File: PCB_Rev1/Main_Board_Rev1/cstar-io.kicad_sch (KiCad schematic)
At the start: 11 parts, among them J2 Conn_01x04_Socket, J3 691137710002, Q1 AO3400A, Q2 AO3400A, Q3 AO3400A, Q4 IRFHM9331TRPBF

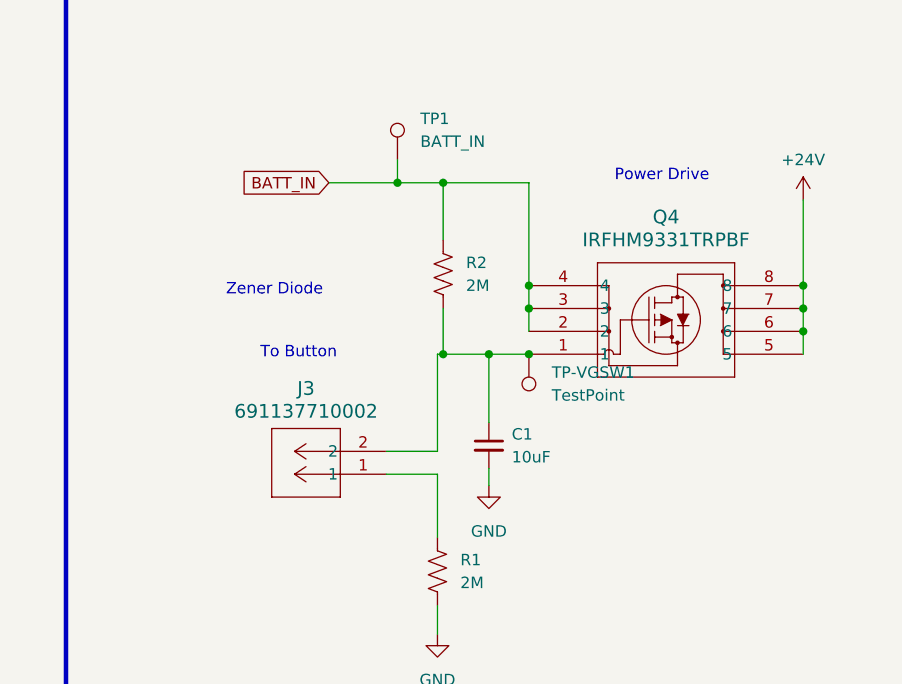
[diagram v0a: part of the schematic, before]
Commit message: I/O footprints added
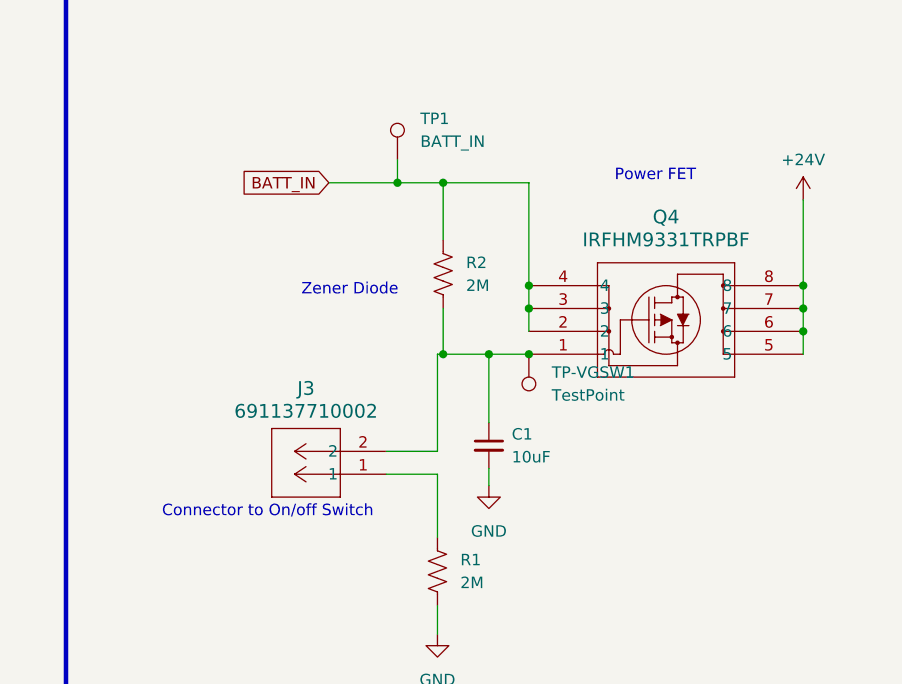
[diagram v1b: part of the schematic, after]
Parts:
- Q1, Q2, Q3: footprint Package_TO_SOT_SMD:SOT-23 -> Footprints:RGB-FETS
- Q4: footprint CSTAR-MainBoard-Footprints:IRFHM9331TRPBF -> Footprints:Power_FET
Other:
- note added: "Connector to On/off Switch"
- note added: "Power FET"
- note removed: "Power Drive"
- note removed: "To Button"
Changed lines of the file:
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@@
 	(text "Zener Diode"
 		(exclude_from_sim no)
-		(at 185.42 64.77 0)
+		(at 193.802 64.77 0)
 		(effects
 			(font
@@
 		)
 	)
-	(text "Power Drive\n"
+	(text "Power FET"
 		(exclude_from_sim no)
 		(at 228.6 52.07 0)
@@
 		)
 	)
-	(text "To Button\n"
-		(exclude_from_sim no)
-		(at 189.23 71.755 0)
+	(text "Connector to On/off Switch"
+		(exclude_from_sim no)
+		(at 178.308 89.408 0)
 		(effects
 			(font
@@
 			)
 		)
-		(property "Footprint" "Package_TO_SOT_SMD:SOT-23"
+		(property "Footprint" "Footprints:RGB-FETS"
 			(at 69.85 62.865 0)
 			(effects
@@
 			)
 		)
-		(property "Footprint" "CSTAR-MainBoard-Footprints:IRFHM9331TRPBF"
+		(property "Footprint" "Footprints:Power_FET"
 			(at 219.075 63.5 0)
 			(effects
@@
 			)
 		)
-		(property "Footprint" "Package_TO_SOT_SMD:SOT-23"
+		(property "Footprint" "Footprints:RGB-FETS"
 			(at 119.38 100.33 0)
 			(effects
@@
 			)
 		)
-		(property "Footprint" "Package_TO_SOT_SMD:SOT-23"
+		(property "Footprint" "Footprints:RGB-FETS"
 			(at 95.25 83.82 0)
 			(effects

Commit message: Added new footprints
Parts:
- J2: footprint CSTAR-MainBoard-Footprints:B4B_PH_K_S -> (none)
- J3: footprint CSTAR-MainBoard-Footprints:691137710002-2CONN -> (none)
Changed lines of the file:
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@@
 			)
 		)
-		(property "Footprint" "CSTAR-MainBoard-Footprints:691137710002-2CONN"
+		(property "Footprint" ""
 			(at 203.2 84.455 0)
 			(effects
@@
 			)
 		)
-		(property "Footprint" "CSTAR-MainBoard-Footprints:B4B_PH_K_S"
+		(property "Footprint" ""
 			(at 130.81 53.975 0)
 			(effects

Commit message: more footprints changes
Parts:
- J3: footprint (none) -> Footprints:691137710002-2CONN
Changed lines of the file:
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@@
 			)
 		)
-		(property "Footprint" ""
+		(property "Footprint" "Footprints:691137710002-2CONN"
 			(at 203.2 84.455 0)
 			(effects

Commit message: FOOTPRINTS COMPLETE!!!!!
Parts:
- J2: footprint (none) -> Footprints:EncoderConn
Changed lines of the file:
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@@
 			)
 		)
-		(property "Footprint" ""
+		(property "Footprint" "Footprints:EncoderConn"
 			(at 130.81 53.975 0)
 			(effects
